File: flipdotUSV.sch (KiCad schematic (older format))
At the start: 23 parts, among them IC1 ATTINY85-P, P2 CONN_01X02, P3 Raspberry_Pi_+_Conn, P4 CONN_01X02, Q1 BC547, U1 LM2596S-5

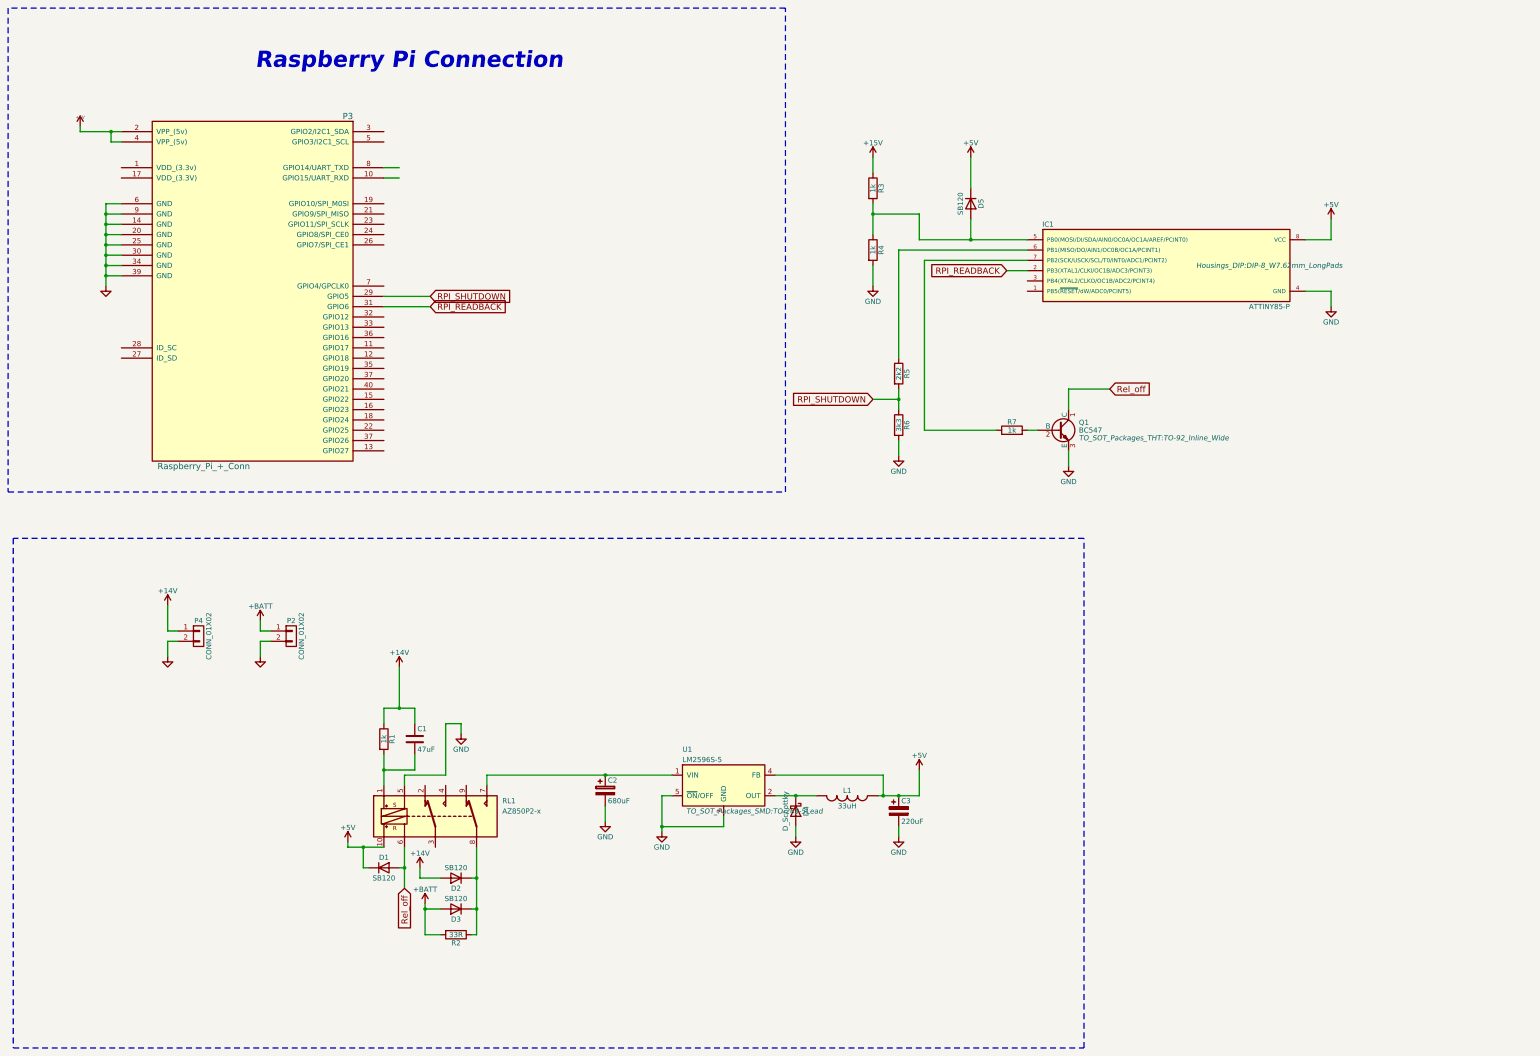
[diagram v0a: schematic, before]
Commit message: added voltage measurement
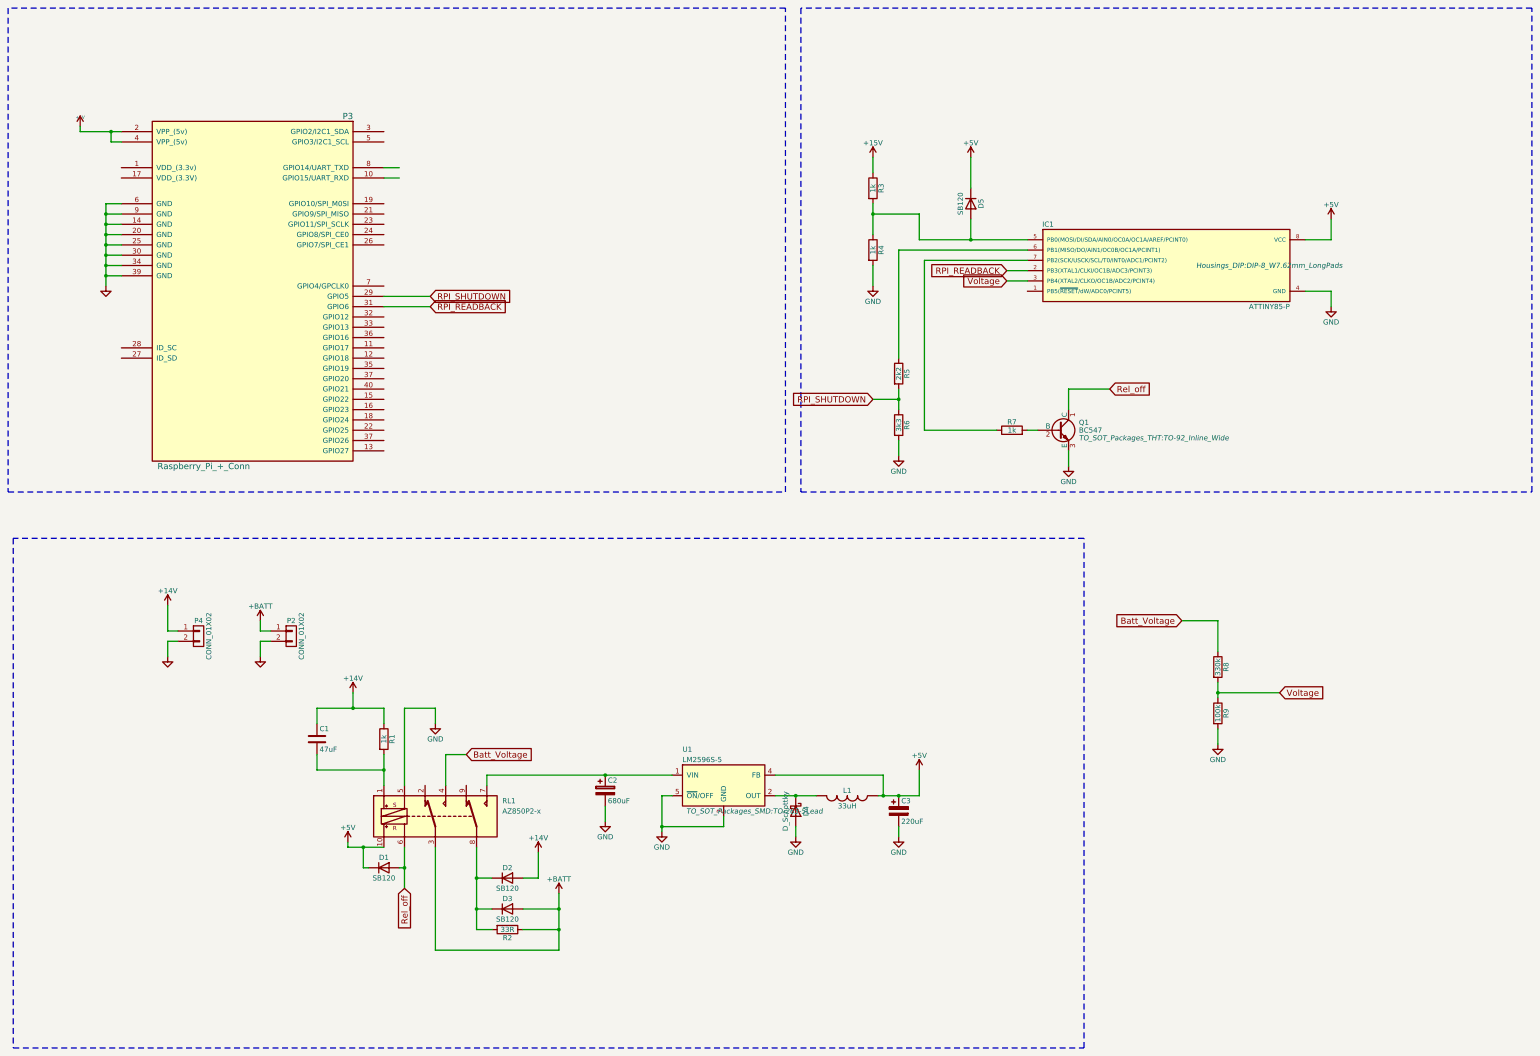
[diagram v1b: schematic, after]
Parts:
- added R8: 330k, symbol R
- added R9: 100k, symbol R
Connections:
- net +BATT: now also R2.1, RL1.3; no longer R2.2
- net GND: now also R9.2
- net Batt_Voltage: now reaches RL1.4
- net Batt_Voltage: now also R8.1
- net at D2.1 (K), D3.1 (K), RL1.8: now also R2.2; no longer R2.1
- net Voltage: now reaches IC1.3 (PB4(XTAL2/CLKO/OC1B/ADC2/PCINT4))
- net Voltage: now also R8.2, R9.1
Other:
- note removed: "Raspberry Pi Connection"
- moved on the sheet: C1, D2, D3, R2

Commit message: add Layout
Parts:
- removed C1: 47uF, Capacitors_SMD:C_0805_HandSoldering, symbol C
- removed IC1: ATTINY85-P, Housings_DIP:DIP-8_W7.62mm_LongPads, symbol ATTINY85-P
- removed RL1: AZ850P2-x, symbol AZ850P2-x
- added C1: 47uF, Capacitors_SMD:CP_Elec_10x10, symbol CP
- added C4: 10n, Capacitors_SMD:C_0805_HandSoldering, symbol C
- added C5: 100n, Capacitors_SMD:C_0805_HandSoldering, symbol C
- added C6: DNL, Capacitors_SMD:CP_Elec_10x10, symbol CP
- added C7: 100nF, Capacitors_SMD:C_0805_HandSoldering, symbol C
- added IC1: ATTINY13-S, SMD_Packages:SOIC-8-N, symbol ATTINY13-S
- added RL1: HFD2-L2, HFD2-L2:HFD2-L2, symbol HFD2-L2
- C2: value 680uF -> 1mF; footprint Capacitors_SMD:c_elec_4x5.8 -> Capacitors_SMD:CP_Elec_10x10
- C3: value 220uF -> 1mF; footprint Capacitors_SMD:c_elec_4x5.8 -> Capacitors_SMD:CP_Elec_10x10
- D1, D2, D3, D5: footprint Diodes_SMD:MiniMELF_Handsoldering -> Diodes_SMD:D_SMA_Handsoldering
- D4: footprint Diodes_SMD:MiniMELF_Handsoldering -> Diodes_SMD:D_SMB-SMC_Universal_Handsoldering
- L1: footprint Inductors:SELF-WE-PD-XXL -> Choke_SMD:Choke_SMD_12x12mm_h8mm; symbol INDUCTOR -> INDUCTOR-RESCUE-flipdotUSV
- P2, P4: footprint Connect:PINHEAD1-2 -> Connect:AK300-2
- R2: footprint Resistors_SMD:R_0805_HandSoldering -> Resistors_ThroughHole:R_Axial_Power_L25.0mm_W6.4mm_P30.48mm
- R8, R9: footprint (none) -> Resistors_SMD:R_0805_HandSoldering
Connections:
- net +15V is gone; now on net +14V: R3.1
- net +14V: now also C1.1
- net +5V: now also C4.1, C5.1, C6.1, C7.1, IC1.8 (VCC), RL1.2
- net +BATT: now also RL1.4
- net Batt_Voltage: now also RL1.8
- net GND: now also C4.2, C5.2, C6.2, C7.2, IC1.4 (GND), RL1.16
- net RPI_READBACK: now also P3.11 (GPIO17), IC1.2 (PB3(CLKI/ADC3/PCINT3)); no longer P3.31 (GPIO6)
- net RPI_SHUTDOWN: now also P3.13 (GPIO27); no longer P3.29 (GPIO5)
- net Rel_off: now also RL1.15
- net Voltage: now also IC1.3 (PB4(ADC2/PCINT4))
- net at C2.1, U1.1 (VIN): now also RL1.9
- net at R1.2: now also C1.2, RL1.1
- net at D2.1 (K), D3.1 (K), R2.2: now also RL1.13
- net at D5.2 (A), R3.2, R4.1: now also IC1.5 (PB0(MOSI/AIN0/OC0A/PCINT0))
- net at R5.1: now also IC1.6 (PB1(MISO/AIN1/OC0B/INT0/PCINT1))
- net at R7.1: now also IC1.7 (PB2(SCK/ADC1/T0/PCINT2))

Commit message: add isp port
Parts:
- added CON?: AVR-ISP-6, AVR-ISP-6, symbol AVR-ISP-6
- IC1: footprint SMD_Packages:SOIC-8-N -> Housings_SOIC:SOIJ-8_5.3x5.3mm_Pitch1.27mm
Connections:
- net labels added: RST, miso, mosi, sck
- wire segments 102 -> 113
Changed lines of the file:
@@
 	9450 3100 10500 3100
 Wire Wire Line
-	9450 3100 9450 2850
-Wire Wire Line
-	9450 2850 9000 2850
+	9450 2850 9450 3100
+Wire Wire Line
+	8750 2850 9450 2850
 Connection ~ 9000 2850
 Wire Wire Line
@@
 F 0 "IC1" H 10700 3750 50  0000 C CNN
 F 1 "ATTINY13-S" H 12150 2950 50  0000 C CNN
-F 2 "SMD_Packages:SOIC-8-N" H 12150 3350 50  0000 C CIN
+F 2 "Housings_SOIC:SOIJ-8_5.3x5.3mm_Pitch1.27mm" H 12150 3350 50  0000 C CIN
 F 3 "" H 10700 3700 50  0000 C CNN
 	1    11500 3350
@@
 	1    0    0    -1
 $EndComp
+$Comp
+L AVR-ISP-6 CON?
+U 1 1 58CE973B
+P 13000 4400
+F 0 "CON?" H 12895 4640 50  0000 C CNN
+F 1 "AVR-ISP-6" H 12735 4170 50  0000 L BNN
+F 2 "AVR-ISP-6" V 12480 4440 50  0001 C CNN
+F 3 "" H 12975 4400 50  0000 C CNN
+	1    13000 4400
+	1    0    0    -1
+$EndComp
+$Comp
+L +5V #PWR?
+U 1 1 58CE9856
+P 13300 4150
+F 0 "#PWR?" H 13300 4000 50  0001 C CNN
+F 1 "+5V" H 13300 4290 50  0000 C CNN
+F 2 "" H 13300 4150 50  0000 C CNN
+F 3 "" H 13300 4150 50  0000 C CNN
+	1    13300 4150
+	1    0    0    -1
+$EndComp
+$Comp
+L GND #PWR?
+U 1 1 58CE98BB
+P 13400 4650
+F 0 "#PWR?" H 13400 4400 50  0001 C CNN
+F 1 "GND" H 13400 4500 50  0000 C CNN
+F 2 "" H 13400 4650 50  0000 C CNN
+F 3 "" H 13400 4650 50  0000 C CNN
+	1    13400 4650
+	1    0    0    -1
+$EndComp
+Wire Wire Line
+	10500 3600 10300 3600
+Text GLabel 10300 3600 0    60   Input ~ 0
+RST
+Wire Wire Line
+	12850 4500 12400 4500
+Wire Wire Line
+	12850 4400 12400 4400
+Wire Wire Line
+	12850 4300 12400 4300
+Wire Wire Line
+	13100 4400 13600 4400
+Wire Wire Line
+	13100 4300 13300 4300
+Wire Wire Line
+	13300 4300 13300 4150
+Wire Wire Line
+	13100 4500 13400 4500
+Wire Wire Line
+	13400 4500 13400 4650
+Text GLabel 12400 4500 0    60   Input ~ 0
+RST
+Wire Wire Line
+	9850 4050 9500 4050
+Connection ~ 9500 4050
+Text GLabel 9850 4050 2    60   Input ~ 0
+sck
+Text GLabel 12400 4400 0    60   Input ~ 0
+sck
+Wire Wire Line
+	9000 4000 9250 4000
+Connection ~ 9250 4000
+Text GLabel 9000 4000 0    60   Input ~ 0
+miso
+Text GLabel 12400 4300 0    60   Input ~ 0
+miso
+Text GLabel 8750 2850 0    60   Input ~ 0
+mosi
+Text GLabel 13600 4400 2    60   Input ~ 0
+mosi
 $EndSCHEMATC
